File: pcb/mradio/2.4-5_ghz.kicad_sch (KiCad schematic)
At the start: 25 parts, among them J501 MDT420E01001, U502 SN74LVC1T45DRL

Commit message: Update some footprints
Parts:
- TP501, TP502, TP503: footprint Package_DFN_QFN:Diodes_UDFN3810-9_TYPE_B -> TestPoint:TestPoint_Loop_D2.60mm_Drill0.9mm_Beaded
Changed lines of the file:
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@@
 			)
 		)
-		(property "Footprint" "Package_DFN_QFN:Diodes_UDFN3810-9_TYPE_B"
+		(property "Footprint" "TestPoint:TestPoint_Loop_D2.60mm_Drill0.9mm_Beaded"
 			(at 121.92 69.85 0)
 			(hide yes)
@@
 			)
 		)
-		(property "Footprint" "Package_DFN_QFN:Diodes_UDFN3810-9_TYPE_B"
+		(property "Footprint" "TestPoint:TestPoint_Loop_D2.60mm_Drill0.9mm_Beaded"
 			(at 162.56 105.41 0)
 			(hide yes)
@@
 			)
 		)
-		(property "Footprint" "Package_DFN_QFN:Diodes_UDFN3810-9_TYPE_B"
+		(property "Footprint" "TestPoint:TestPoint_Loop_D2.60mm_Drill0.9mm_Beaded"
 			(at 121.92 93.98 0)
 			(hide yes)

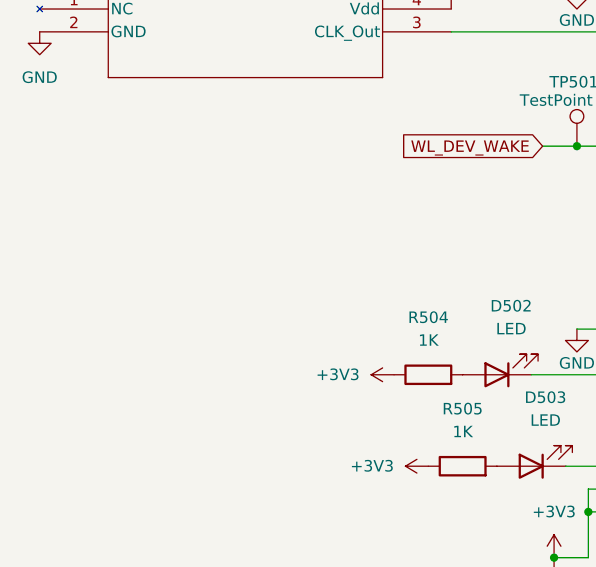
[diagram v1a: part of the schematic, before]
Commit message: Add mounting holes
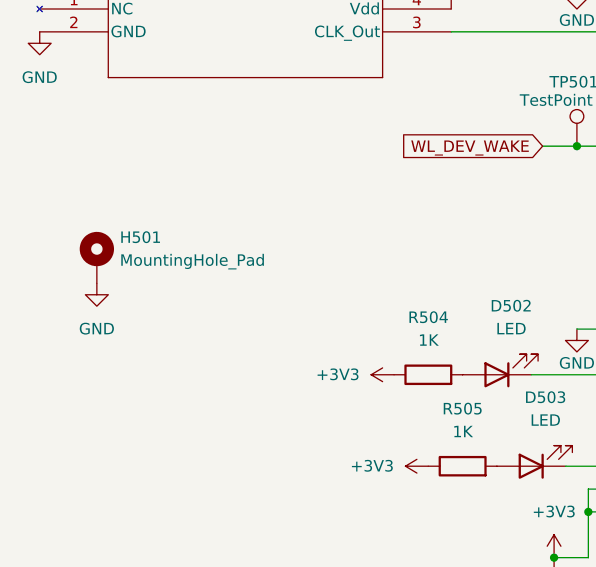
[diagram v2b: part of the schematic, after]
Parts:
- added H501: MountingHole_Pad, MountingHole:MountingHole_2.2mm_M2_ISO7380_Pad, symbol Mechanical:MountingHole_Pad
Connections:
- net GND: now also H501.1
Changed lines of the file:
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@@
+	(symbol
+		(lib_id "power:GND")
+		(at 63.5 109.22 0)
+		(unit 1)
+		(body_style 1)
+		(exclude_from_sim no)
+		(in_bom yes)
+		(on_board yes)
+		(in_pos_files yes)
+		(dnp no)
+		(fields_autoplaced yes)
+		(property "Reference" "#PWR0501"
+			(at 63.5 115.57 0)
+			(hide yes)
+			(show_name no)
+			(do_not_autoplace no)
+			(effects
+				(font
+					(size 1.27 1.27)
+				)
+			)
+		)
+		(property "Value" "GND"
+			(at 63.5 114.3 0)
+			(show_name no)
+			(do_not_autoplace no)
+			(effects
+				(font
+					(size 1.27 1.27)
+				)
+			)
+		)
+		(property "Footprint" ""
+			(at 63.5 109.22 0)
+			(hide yes)
+			(show_name no)
+			(do_not_autoplace no)
+			(effects
+				(font
+					(size 1.27 1.27)
+				)
+			)
+		)
+		(property "Datasheet" ""
+			(at 63.5 109.22 0)
+			(hide yes)
+			(show_name no)
+			(do_not_autoplace no)
+			(effects
+				(font
+					(size 1.27 1.27)
+				)
+			)
+		)
+		(property "Description" "Power symbol creates a global label with name \"GND\" , ground"
+			(at 63.5 109.22 0)
+			(hide yes)
+			(show_name no)
+			(do_not_autoplace no)
+			(effects
+				(font
+					(size 1.27 1.27)
+				)
+			)
+		)
+		(pin "1"
+		)
+		(instances
+			(project "mradio"
+				(path "/a3cfb3f7-0a76-4383-aac7-b46c1ac4283d"
+					(reference "#PWR0501")
+					(unit 1)
+				)
+			)
+		)
+	)
 	(symbol
 		(lib_id "power:GND")
@@
 					(unit 1)
 				)
+			)
+		)
+	)
+	(symbol
+		(lib_id "Mechanical:MountingHole_Pad")
+		(at 63.5 106.68 0)
+		(unit 1)
+		(body_style 1)
+		(exclude_from_sim no)
+		(in_bom no)
+		(on_board yes)
+		(in_pos_files yes)
+		(dnp no)
+		(fields_autoplaced yes)
+		(property "Reference" "H501"
+			(at 66.04 104.1399 0)
+			(show_name no)
+			(do_not_autoplace no)
+			(effects
+				(font
+					(size 1.27 1.27)
+				)
+				(justify left)
+			)
+		)
+		(property "Value" "MountingHole_Pad"
+			(at 66.04 106.6799 0)
+			(show_name no)
+			(do_not_autoplace no)
+			(effects
+				(font
+					(size 1.27 1.27)
+				)
+				(justify left)
+			)
+		)
+		(property "Footprint" "MountingHole:MountingHole_2.2mm_M2_ISO7380_Pad"
+			(at 63.5 106.68 0)
+			(hide yes)
+			(show_name no)
+			(do_not_autoplace no)
+			(effects
+				(font
+					(size 1.27 1.27)
+				)
+			)
+		)
+		(property "Datasheet" ""
+			(at 63.5 106.68 0)
+			(hide yes)
+			(show_name no)
+			(do_not_autoplace no)
+			(effects
+				(font
+					(size 1.27 1.27)
+				)
+			)
+		)
+		(property "Description" "Mounting Hole with connection"
+			(at 63.5 106.68 0)
+			(hide yes)
+			(show_name no)
+			(do_not_autoplace no)
+			(effects
+				(font
+					(size 1.27 1.27)
+				)
+			)
+		)
+		(pin "1"
+		)
+		(instances
+			(project "mradio"
+				(path "/a3cfb3f7-0a76-4383-aac7-b46c1ac4283d"
+					(reference "H501")
+					(unit 1)
+				)

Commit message: make test points smaller
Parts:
- TP501, TP502, TP503: footprint TestPoint:TestPoint_Loop_D2.60mm_Drill0.9mm_Beaded -> TestPoint:TestPoint_Loop_D1.80mm_Drill1.0mm_Beaded
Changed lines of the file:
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@@
 			)
 		)
-		(property "Footprint" "TestPoint:TestPoint_Loop_D2.60mm_Drill0.9mm_Beaded"
+		(property "Footprint" "TestPoint:TestPoint_Loop_D1.80mm_Drill1.0mm_Beaded"
 			(at 121.92 69.85 0)
 			(hide yes)
@@
 			)
 		)
-		(property "Footprint" "TestPoint:TestPoint_Loop_D2.60mm_Drill0.9mm_Beaded"
+		(property "Footprint" "TestPoint:TestPoint_Loop_D1.80mm_Drill1.0mm_Beaded"
 			(at 162.56 105.41 0)
 			(hide yes)
@@
 			)
 		)
-		(property "Footprint" "TestPoint:TestPoint_Loop_D2.60mm_Drill0.9mm_Beaded"
+		(property "Footprint" "TestPoint:TestPoint_Loop_D1.80mm_Drill1.0mm_Beaded"
 			(at 121.92 93.98 0)
 			(hide yes)

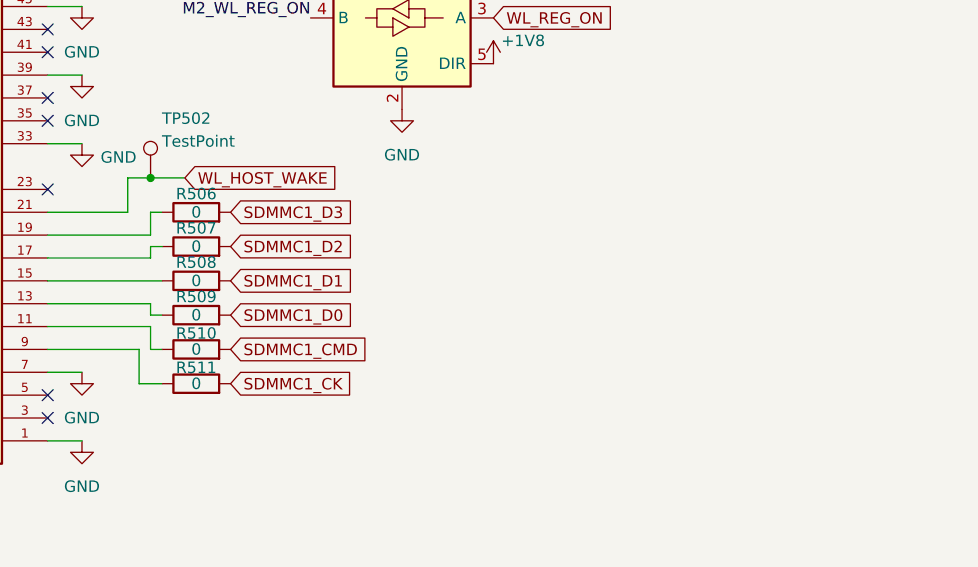
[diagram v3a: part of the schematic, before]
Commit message: update stackup and wifi net class
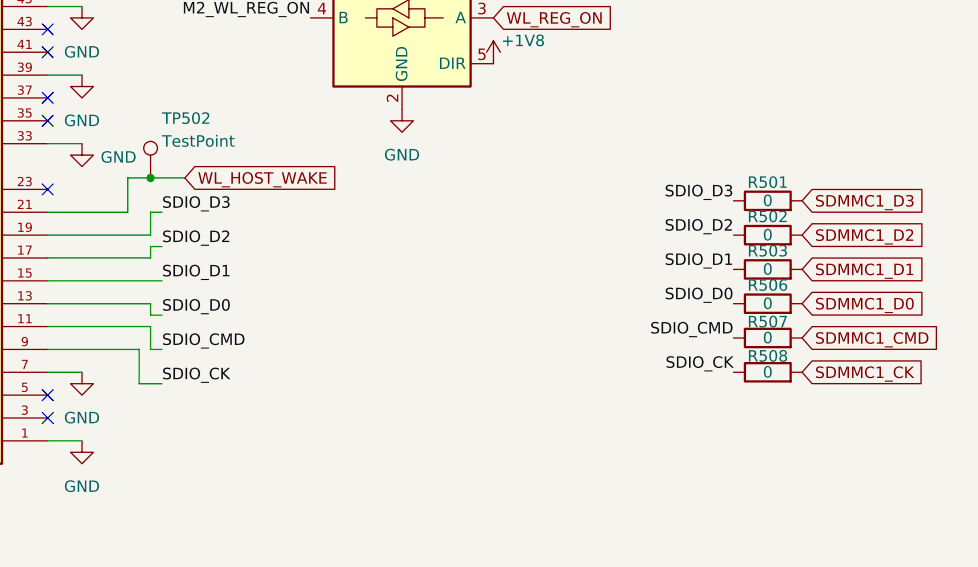
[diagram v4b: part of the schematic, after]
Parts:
- removed R509, R510, R511: 0, Resistor_SMD:R_0603_1608Metric, symbol Device:R
- added R501, R502, R503: 0, Resistor_SMD:R_0603_1608Metric, symbol Device:R
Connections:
- net SDMMC1_CK: now also R508.2
- net SDMMC1_CMD: now also R507.2
- net SDMMC1_D0: now also R506.2
- net SDMMC1_D1: now also R503.2; no longer R508.2
- net SDMMC1_D2: now also R502.2; no longer R507.2
- net SDMMC1_D3: now also R501.2; no longer R506.2
- net SDIO_D0: now reaches J501.13
- net SDIO_D0: now also R506.1
- net SDIO_D3: now reaches J501.19
- net SDIO_D3: now also R501.1; no longer R506.1
- net SDIO_CMD: now reaches J501.11
- net SDIO_CMD: now also R507.1
- net SDIO_CK: now reaches R508.1
- net SDIO_CK: now also J501.9; no longer J501.15
- net SDIO_D2: now reaches J501.17
- net SDIO_D2: now also R502.1; no longer R507.1
- new net SDIO_D1: J501.15, R503.1

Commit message: work on SDIO a bit
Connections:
- net SDIO_CMD: now also R516.2
- net SDIO_D0: now also R512.2
- net SDIO_D1: now also R513.2
- net SDIO_D2: now also R514.2
- net SDIO_D3: now also R515.2
- net SDMMC1_CMD: no longer R516.2
- net SDMMC1_D0: no longer R512.2
- net SDMMC1_D1: no longer R513.2
- net SDMMC1_D2: no longer R514.2
- net SDMMC1_D3: no longer R515.2
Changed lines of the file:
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@@
+		)
+	)
+	(label "SDIO_D3"
+		(at 194.31 50.8 270)
+		(effects
+			(font
+				(size 1.27 1.27)
+			)
+			(justify right bottom)
+		)
+	)
+	(label "SDIO_CMD"
+		(at 203.2 50.8 270)
+		(effects
+			(font
+				(size 1.27 1.27)
+			)
+			(justify right bottom)
 		)
 	)
@@
 		)
 	)
+	(label "SDIO_D2"
+		(at 185.42 50.8 270)
+		(effects
+			(font
+				(size 1.27 1.27)
+			)
+			(justify right bottom)
+		)
+	)
 	(label "SDIO_D3"
 		(at 158.75 109.22 0)
@@
 		)
 	)
+	(label "SDIO_D1"
+		(at 176.53 50.8 270)
+		(effects
+			(font
+				(size 1.27 1.27)
+			)
+			(justify right bottom)
+		)
+	)
 	(label "M2_WL_REG_ON"
 		(at 113.03 69.85 180)
@@
 		)
 	)
+	(label "SDIO_D0"
+		(at 167.64 50.8 270)
+		(effects
+			(font
+				(size 1.27 1.27)
+			)
+			(justify right bottom)
+		)
+	)
 	(label "M2_WL_REG_ON"
 		(at 175.26 87.63 180)
@@
 	(global_label "SDMMC1_CMD"
 		(shape input)
-		(at 203.2 50.8 270)
-		(fields_autoplaced yes)
-		(effects
-			(font
-				(size 1.27 1.27)
-			)
-			(justify right)
-		)
-		(property "Intersheetrefs" "${INTERSHEET_REFS}"
-			(at 203.2 66.606 90)
-			(hide yes)
-			(show_name no)
-			(do_not_autoplace no)
-			(effects
-				(font
-					(size 1.27 1.27)
-				)
-				(justify right)
-			)
-		)
-	)
-	(global_label "SDMMC1_CMD"
-		(shape input)
 		(at 229.87 123.19 0)
 		(fields_autoplaced yes)
@@
 			)
 		)
-	)
-	(global_label "SDMMC1_D2"
-		(shape input)
-		(at 185.42 50.8 270)
-		(fields_autoplaced yes)
-		(effects
-			(font
-				(size 1.27 1.27)
-			)
-			(justify right)
-		)
-		(property "Intersheetrefs" "${INTERSHEET_REFS}"
-			(at 185.42 65.0941 90)
-			(hide yes)
-			(show_name no)
-			(do_not_autoplace no)
-			(effects
-				(font
-					(size 1.27 1.27)
-				)
-				(justify right)
-			)
-		)
-	)
-	(global_label "SDMMC1_D1"
-		(shape input)
-		(at 176.53 50.8 270)
-		(fields_autoplaced yes)
-		(effects
-			(font
-				(size 1.27 1.27)
-			)
-			(justify right)
-		)
-		(property "Intersheetrefs" "${INTERSHEET_REFS}"
-			(at 176.53 65.0941 90)
-			(hide yes)
-			(show_name no)
-			(do_not_autoplace no)
-			(effects
-				(font
-					(size 1.27 1.27)
-				)
-				(justify right)
-			)
-		)
-	)
-	(global_label "SDMMC1_D3"
-		(shape input)
-		(at 194.31 50.8 270)
-		(fields_autoplaced yes)
-		(effects
-			(font
-				(size 1.27 1.27)
-			)
-			(justify right)
-		)
-		(property "Intersheetrefs" "${INTERSHEET_REFS}"
-			(at 194.31 65.0941 90)
-			(hide yes)
-			(show_name no)
-			(do_not_autoplace no)
-			(effects
-				(font
-					(size 1.27 1.27)
-				)
-				(justify right)
-			)
-		)
-	)
-	(global_label "SDMMC1_D0"
-		(shape input)
-		(at 167.64 50.8 270)
-		(fields_autoplaced yes)
-		(effects
-			(font
-				(size 1.27 1.27)
-			)
-			(justify right)
-		)
-		(property "Intersheetrefs" "${INTERSHEET_REFS}"
-			(at 167.64 65.0941 90)
-			(hide yes)
-			(show_name no)
-			(do_not_autoplace no)
-			(effects
-				(font
-					(size 1.27 1.27)
-				)
-				(justify right)
-			)
-		)
